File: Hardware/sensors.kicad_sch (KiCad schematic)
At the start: 29 parts, among them IC1 BMP388, J1 Conn_Coaxial, J12 Conn_Coaxial, U13 LSM6DSO, U2 MAX-M10S, U3 74LVC1GU04

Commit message: schem uzlabojumi
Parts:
- added D2: D_TVS, Diode_SMD:D_SOD-523, symbol Device:D_TVS
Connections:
- net GND: now also D2.1 (A1)
- net at E22-400M22S2.21 (ANT), J1.1 (In): now also D2.2 (A2)
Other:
- moved on the sheet: J1
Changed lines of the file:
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@@
 	)
 	(junction
+		(at 64.77 158.75)
+		(diameter 0)
+		(color 0 0 0 0)
+	)
+	(junction
 		(at 134.62 41.91)
 		(diameter 0)
@@
 	(wire
 		(pts
-			(xy 59.69 165.1) (xy 68.58 165.1)
+			(xy 59.69 158.75) (xy 64.77 158.75)
 		)
 		(stroke
@@
 	(wire
 		(pts
-			(xy 68.58 158.75) (xy 74.93 158.75)
-		)
-		(stroke
-			(width 0)
-			(type default)
-		)
-	)
-	(wire
-		(pts
 			(xy 110.49 133.35) (xy 113.03 133.35)
 		)
@@
 		)
 	)
-	(wire
+	(polyline
 		(pts
-			(xy 54.61 153.67) (xy 54.61 160.02)
+			(xy 176.53 198.12) (xy 176.53 110.49)
 		)
 		(stroke
@@
 		)
 	)
-	(polyline
+	(wire
 		(pts
-			(xy 176.53 198.12) (xy 176.53 110.49)
+			(xy 170.18 68.58) (xy 170.18 73.66)
 		)
 		(stroke
@@
 	(wire
 		(pts
-			(xy 170.18 68.58) (xy 170.18 73.66)
+			(xy 116.84 156.21) (xy 116.84 158.75)
 		)
 		(stroke
@@
 	(wire
 		(pts
-			(xy 116.84 156.21) (xy 116.84 158.75)
+			(xy 64.77 158.75) (xy 74.93 158.75)
 		)
 		(stroke
@@
 	(wire
 		(pts
+			(xy 64.77 158.75) (xy 64.77 160.02)
+		)
+		(stroke
+			(width 0)
+			(type default)
+		)
+	)
+	(wire
+		(pts
 			(xy 200.66 50.8) (xy 209.55 50.8)
 		)
@@
 	(wire
 		(pts
-			(xy 68.58 158.75) (xy 68.58 165.1)
-		)
-		(stroke
-			(width 0)
-			(type default)
-		)
-	)
-	(wire
-		(pts
 			(xy 163.83 73.66) (xy 163.83 76.2)
 		)
@@
 	(wire
 		(pts
-			(xy 74.93 161.29) (xy 74.93 171.45)
+			(xy 74.93 161.29) (xy 74.93 165.1)
 		)
 		(stroke
@@
 	(symbol
 		(lib_id "Connector:Conn_Coaxial")
-		(at 54.61 165.1 180)
+		(at 54.61 158.75 180)
 		(unit 1)
 		(exclude_from_sim no)
@@
 		(fields_autoplaced yes)
 		(property "Reference" "J1"
-			(at 50.8 163.5367 0)
+			(at 50.8 157.1867 0)
 			(effects
 				(font
@@
 		)
 		(property "Value" "Conn_Coaxial"
-			(at 50.8 166.0767 0)
+			(at 50.8 159.7267 0)
 			(effects
 				(font
@@
 		)
 		(property "Footprint" "Connector_Coaxial:SMA_Molex_73251-2200_Horizontal"
-			(at 54.61 165.1 0)
+			(at 54.61 158.75 0)
 			(effects
 				(font
@@
 		)
 		(property "Datasheet" "~"
-			(at 54.61 165.1 0)
+			(at 54.61 158.75 0)
 			(effects
 				(font
@@
 		)
 		(property "Description" "coaxial connector (BNC, SMA, SMB, SMC, Cinch/RCA, LEMO, ...)"
-			(at 54.61 165.1 0)
+			(at 54.61 158.75 0)
 			(effects
 				(font
@@
 	)
 	(symbol
+		(lib_id "power:GND")
+		(at 64.77 167.64 0)
+		(unit 1)
+		(exclude_from_sim no)
+		(in_bom yes)
+		(on_board yes)
+		(dnp no)
+		(fields_autoplaced yes)
+		(property "Reference" "#PWR0140"
+			(at 64.77 173.99 0)
+			(effects
+				(font
+					(size 1.27 1.27)
+				)
+				(hide yes)
+			)
+		)
+		(property "Value" "GND"
+			(at 64.77 172.72 0)
+			(effects
+				(font
+					(size 1.27 1.27)
+				)
+			)
+		)
+		(property "Footprint" ""
+			(at 64.77 167.64 0)
+			(effects
+				(font
+					(size 1.27 1.27)
+				)
+				(hide yes)
+			)
+		)
+		(property "Datasheet" ""
+			(at 64.77 167.64 0)
+			(effects
+				(font
+					(size 1.27 1.27)
+				)
+				(hide yes)
+			)
+		)
+		(property "Description" "Power symbol creates a global label with name \"GND\" , ground"
+			(at 64.77 167.64 0)
+			(effects
+				(font
+					(size 1.27 1.27)
+				)
+				(hide yes)
+			)
+		)
+		(pin "1"
+		)
+		(instances
+			(project "flight_comp"
+				(path "/99100214-bcab-4638-96e7-2342f837a8e5/ccff0650-056e-451f-a7b4-968f0cd07701"
+					(reference "#PWR0140")
+					(unit 1)
+				)
+			)
+		)
+	)
+	(symbol
 		(lib_id "Device:C")
 		(at 130.81 135.89 0)
@@
 	)
 	(symbol
+		(lib_id "Device:D_TVS")
+		(at 64.77 163.83 90)
+		(unit 1)
+		(exclude_from_sim no)
+		(in_bom yes)
+		(on_board yes)
+		(dnp no)
+		(fields_autoplaced yes)
+		(property "Reference" "D2"
+			(at 58.42 163.83 0)
+			(effects
+				(font
+					(size 1.27 1.27)
+				)
+			)
+		)
+		(property "Value" "D_TVS"
+			(at 60.96 163.83 0)
+			(effects
+				(font
+					(size 1.27 1.27)
+				)
+			)
+		)
+		(property "Footprint" "Diode_SMD:D_SOD-523"
+			(at 64.77 163.83 0)
+			(effects
+				(font
+					(size 1.27 1.27)
+				)
+				(hide yes)
+			)
+		)
+		(property "Datasheet" "~"
+			(at 64.77 163.83 0)
+			(effects
+				(font
+					(size 1.27 1.27)
+				)
+				(hide yes)
+			)
+		)
+		(property "Description" "Bidirectional transient-voltage-suppression diode"
+			(at 64.77 163.83 0)
+			(effects
+				(font
+					(size 1.27 1.27)
+				)
+				(hide yes)
+			)
+		)
+		(pin "2"
+		)
+		(pin "1"
+		)
+		(instances
+			(project "flight_comp"
+				(path "/99100214-bcab-4638-96e7-2342f837a8e5/ccff0650-056e-451f-a7b4-968f0cd07701"
+					(reference "D2")
+					(unit 1)
+				)
+			)
+		)
+	)
+	(symbol
 		(lib_id "Device:C_Small")
 		(at 219.71 63.5 180)
@@
 	(symbol
 		(lib_id "power:GND")
-		(at 74.93 171.45 0)
+		(at 74.93 165.1 0)
 		(unit 1)
 		(exclude_from_sim no)
@@
 		(dnp no)
 		(property "Reference" "#PWR012"
-			(at 74.93 177.8 0)
+			(at 74.93 171.45 0)
 			(effects
 				(font
@@
 		)
 		(property "Value" "GND"
-			(at 72.898 175.514 0)
+			(at 72.898 169.164 0)
 			(effects
 				(font
@@
 		)
 		(property "Footprint" ""
-			(at 74.93 171.45 0)
+			(at 74.93 165.1 0)
 			(effects
 				(font
@@
 		)
 		(property "Datasheet" ""
-			(at 74.93 171.45 0)
+			(at 74.93 165.1 0)
 			(effects
 				(font
@@
 		)
 		(property "Description" "Power symbol creates a global label with name \"GND\" , ground"
-			(at 74.93 171.45 0)
+			(at 74.93 165.1 0)
 			(effects
 				(font

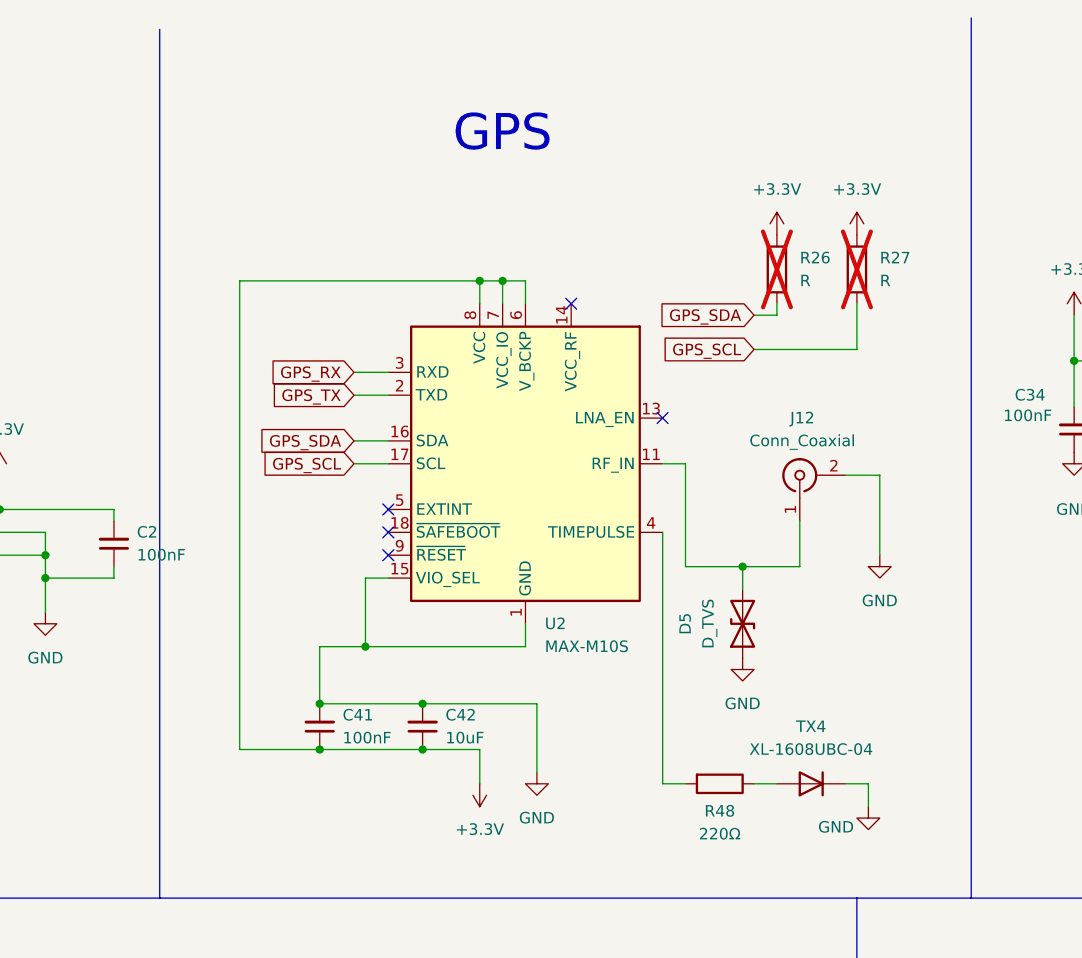
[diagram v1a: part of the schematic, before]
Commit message: GPS antenna connections, pps is connected to the mcu, pps diode replaced
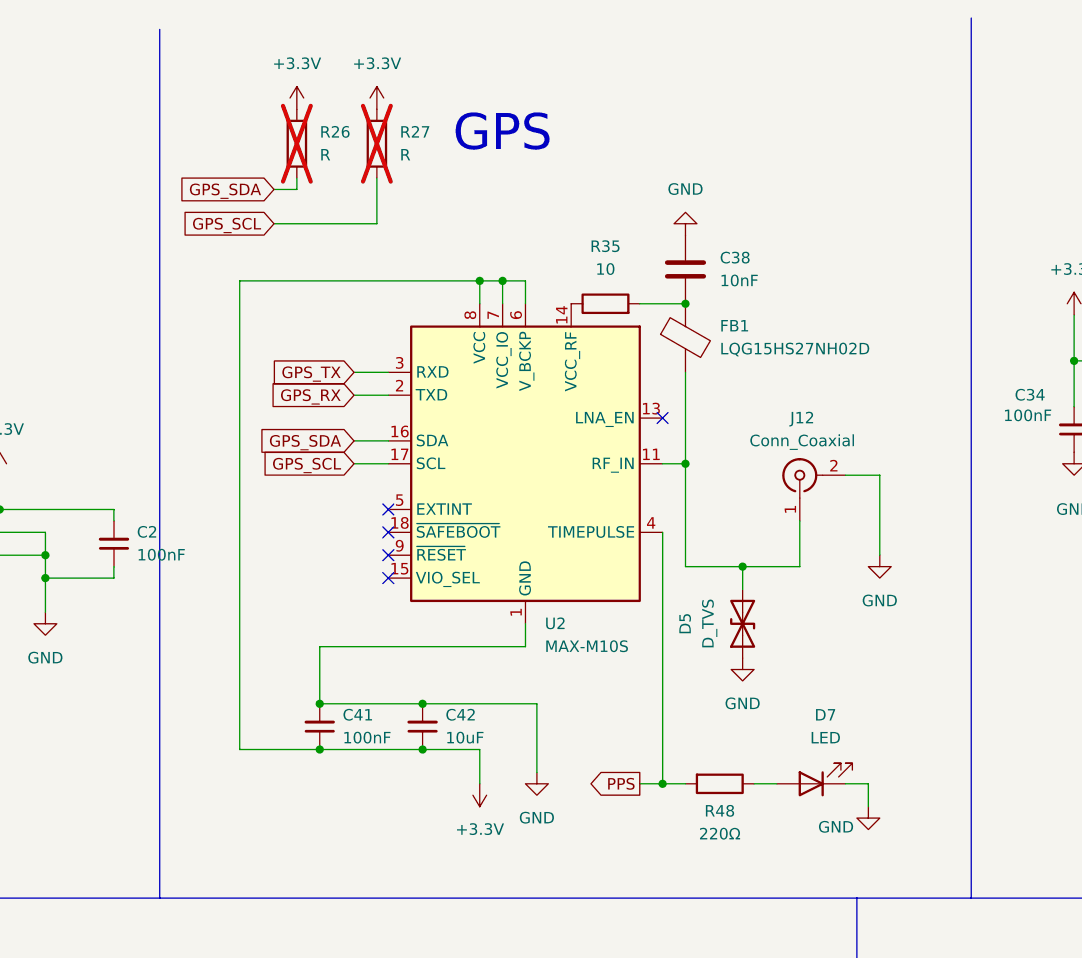
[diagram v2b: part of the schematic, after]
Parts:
- removed TX4: XL-1608UBC-04, LED_SMD:LED_0603_1608Metric, symbol Diode:1SS355VM
- added C38: 10nF, Capacitor_SMD:C_0603_1608Metric, symbol Device:C
- added D7: LED, LED_SMD:LED_0603_1608Metric, symbol Device:LED
- added FB1: LQG15HS27NH02D, Inductor_SMD:L_0402_1005Metric, symbol Device:FerriteBead
- added R35: 10, Resistor_SMD:R_0603_1608Metric, symbol Device:R
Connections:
- net GND: now also C38.2, D7.1 (K); no longer U2.15 (VIO_SEL)
- net GPS_RX: now also U2.2 (TXD); no longer U2.3 (RXD)
- net GPS_TX: now also U2.3 (RXD); no longer U2.2 (TXD)
- net at D5.2 (A2), J12.1 (In), U2.11 (RF_IN): now also FB1.2
- net at R48.1: now also D7.2 (A)
- net PPS: now reaches R48.2, U2.4 (TIMEPULSE)
- net at U2.14 (VCC_RF): now also R35.1
- new net: C38.1, FB1.1, R35.2
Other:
- moved on the sheet: R26, R27
